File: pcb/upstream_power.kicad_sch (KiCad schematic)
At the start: 5 parts, among them J8 USB-C power, U16 HUSB238

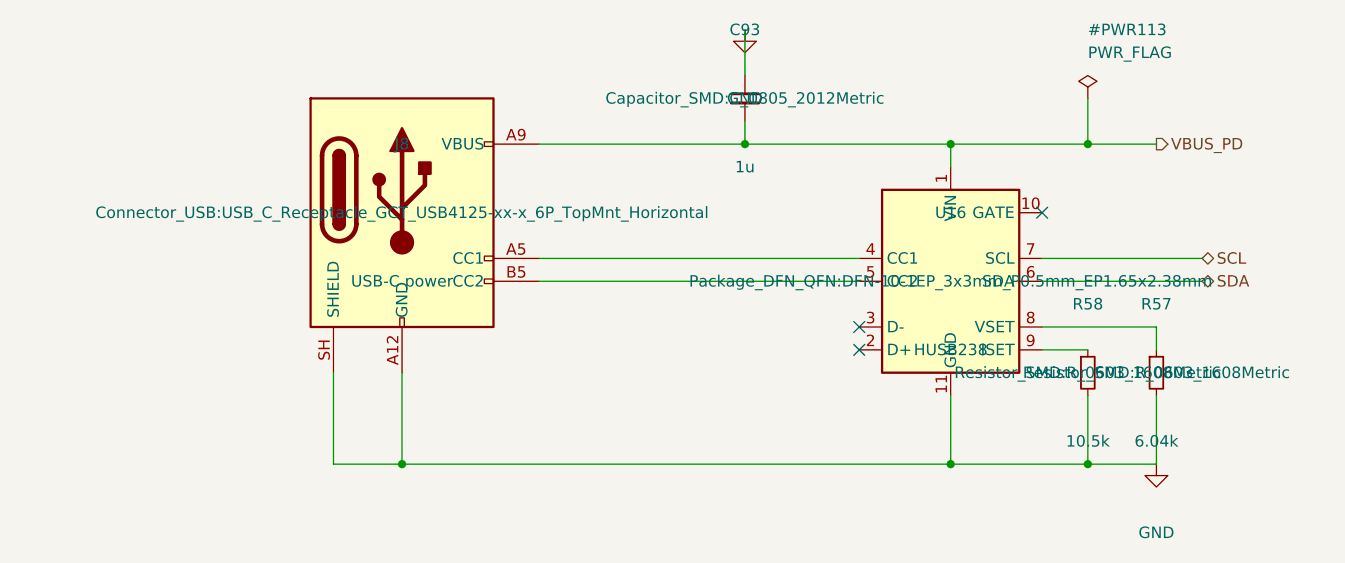
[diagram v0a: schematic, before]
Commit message: checkpoint the battery, PD and radio design as it stood
The last state of the full-featured board before it is reduced to a single
USB-C input: the power block re-placed part by part in order of importance,
the charger's signal pins fanned out, the differential pairs renamed so the
layout tool recognises them, the 3.3 V converter's feedback divider joined
to its pin, the FETs given their part number, and the non-printing fields
hidden on the schematic. The layout is incomplete and is recorded as such.

Co-Authored-By: Claude Fable 5.1 <noreply@anthropic.com>
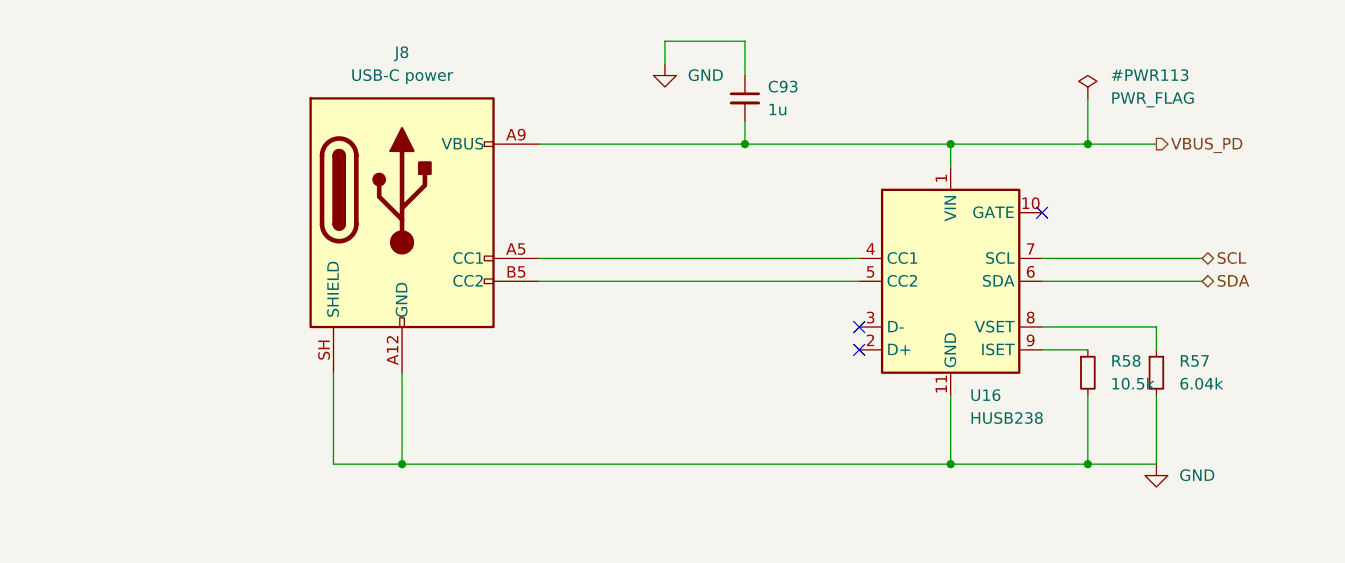
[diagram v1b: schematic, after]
